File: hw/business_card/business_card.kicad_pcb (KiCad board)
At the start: 4 copper layers, 106 x 61.7 mm, 111 parts, among them J1 10164359-00011LF, J2 Conn_01x02_Pin, Q1 2N7002NXAKR, Q2 2N7002NXAKR, Q3 2N7002NXAKR, SW1 3983, SW2 3983, U1 PIC16F15245T-I/REB, U2 MCP7940MT-I/MNY, U3 PCAL6416AHF_128, U4 PCAL6416AHF_128, U5 LM8365BALMF27/NOPB, U6 TMP1075NDRLR, U7 LMV331IDBVRG4, Y1 ECS-327MVATX-2-CN-TR3

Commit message: BoM complete
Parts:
- added TP1: TestPoint, TestPoint:TestPoint_Pad_D2.5mm, B.Cu at (76.0, 71.3)
- added TP2: TestPoint, TestPoint:TestPoint_Pad_D2.5mm, B.Cu at (75.9, 80.9)
- added TP3: TestPoint, TestPoint:TestPoint_Pad_D2.5mm, B.Cu at (75.9, 85.8)
- added TP4: TestPoint, TestPoint:TestPoint_Pad_D2.5mm, B.Cu at (75.9, 76.1)
- added TP5: TestPoint, TestPoint:TestPoint_Pad_D2.5mm, B.Cu at (76.0, 90.7)
- turned R51 to -45 degrees
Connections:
- R51 pad 1: Net-(Q1-G) -> +5V
- R51 pad 2: GND -> Net-(Q1-G)
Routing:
- net /MCU/ICSP.CLK: track 0.00 -> 8.55 mm
- net /MCU/ICSP.MCLR: track 6.37 -> 14.4 mm
- net /MCU/ICSP.DAT: track 0.00 -> 6.88 mm
- net +5V: track 45.2 -> 48.0 mm, vias 31 -> 33
- net GND: track 199.9 -> 200.7 mm, vias 140 -> 141
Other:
- board text added: "+5V"
- board text added: "DAT"
- board text added: "GND"
- board text added: "MCLR"

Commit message: HW work complete
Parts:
- added G***: LOGO, proj:bom_qr, F.Cu at (134.9, 115.1)
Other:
- board text added: "BoM"

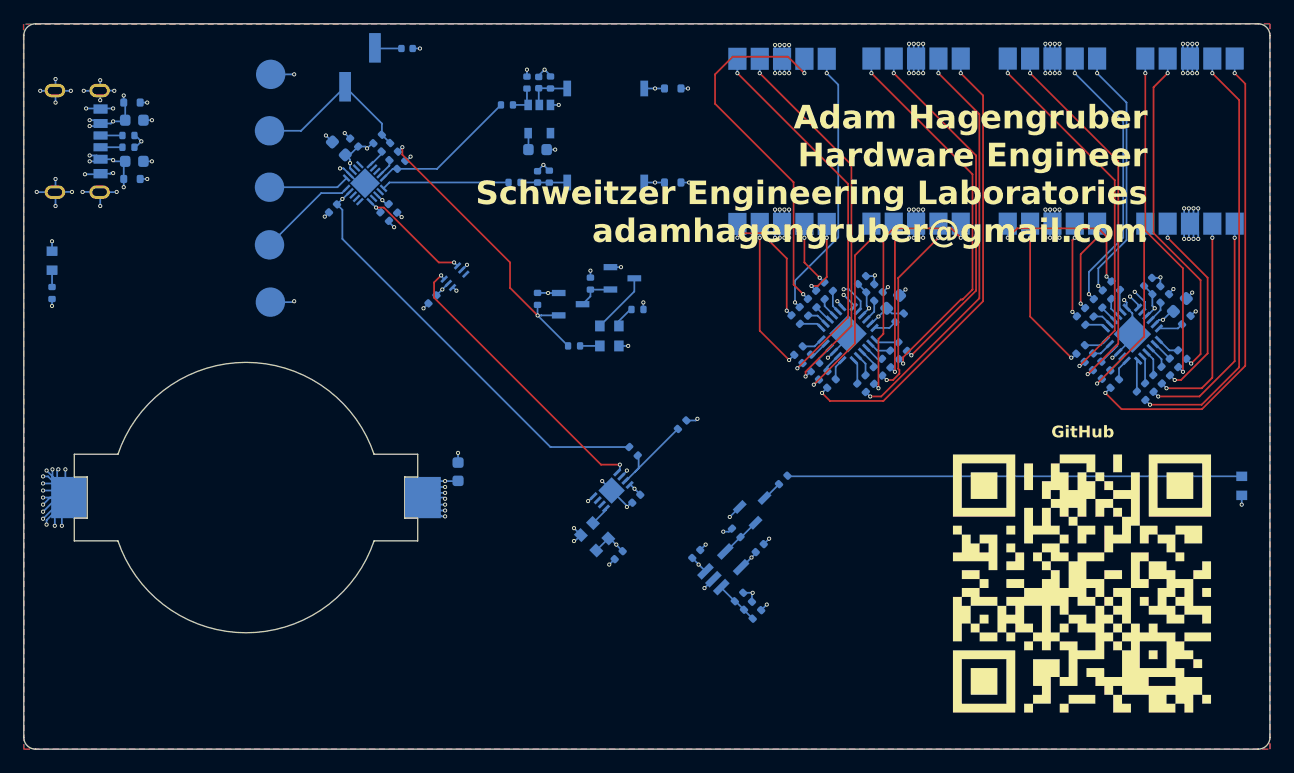
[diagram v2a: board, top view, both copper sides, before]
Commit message: Updated via diameters
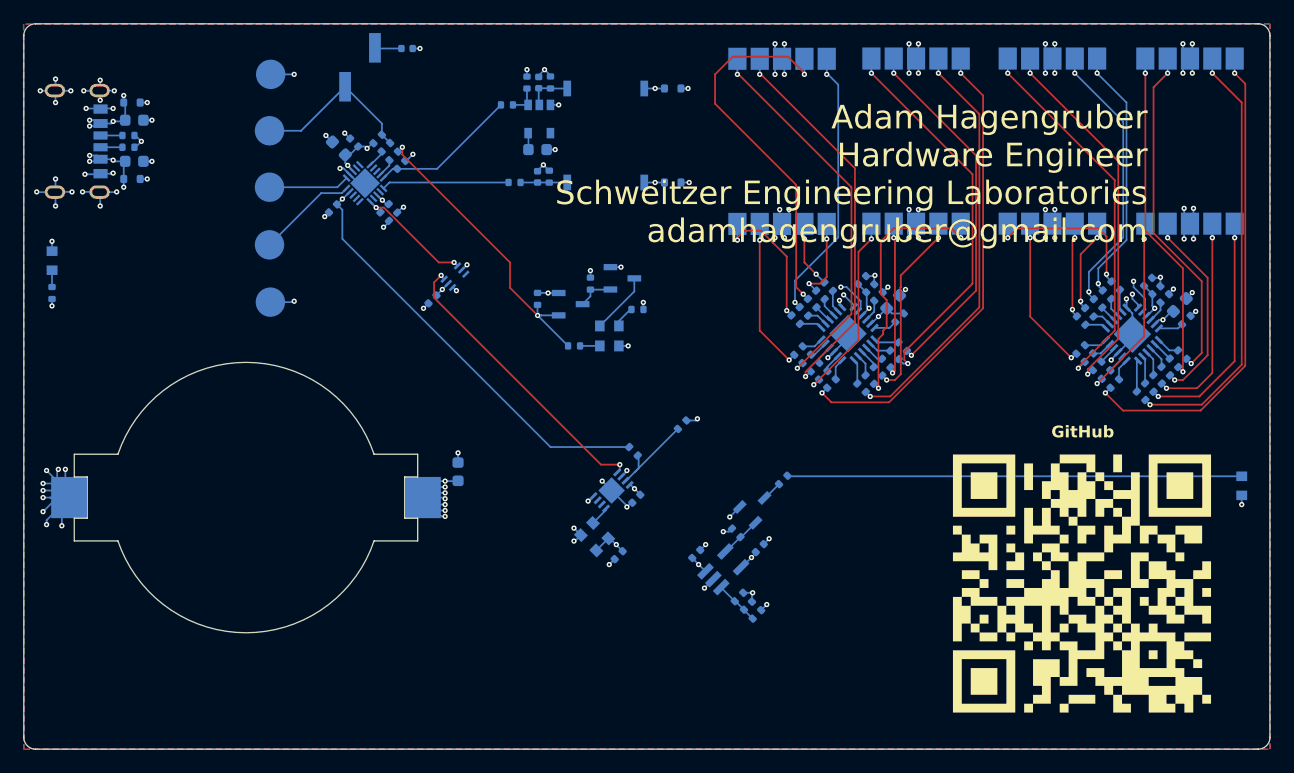
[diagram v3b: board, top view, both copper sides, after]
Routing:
- net GND: track 200.7 -> 166.1 mm, vias 141 -> 104
- net I2C.SDA: track 91.7 -> 93.4 mm
- net Net-(LED4-DP): track 11.4 -> 12.1 mm
